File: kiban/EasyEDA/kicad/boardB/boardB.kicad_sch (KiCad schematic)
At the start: 0 parts

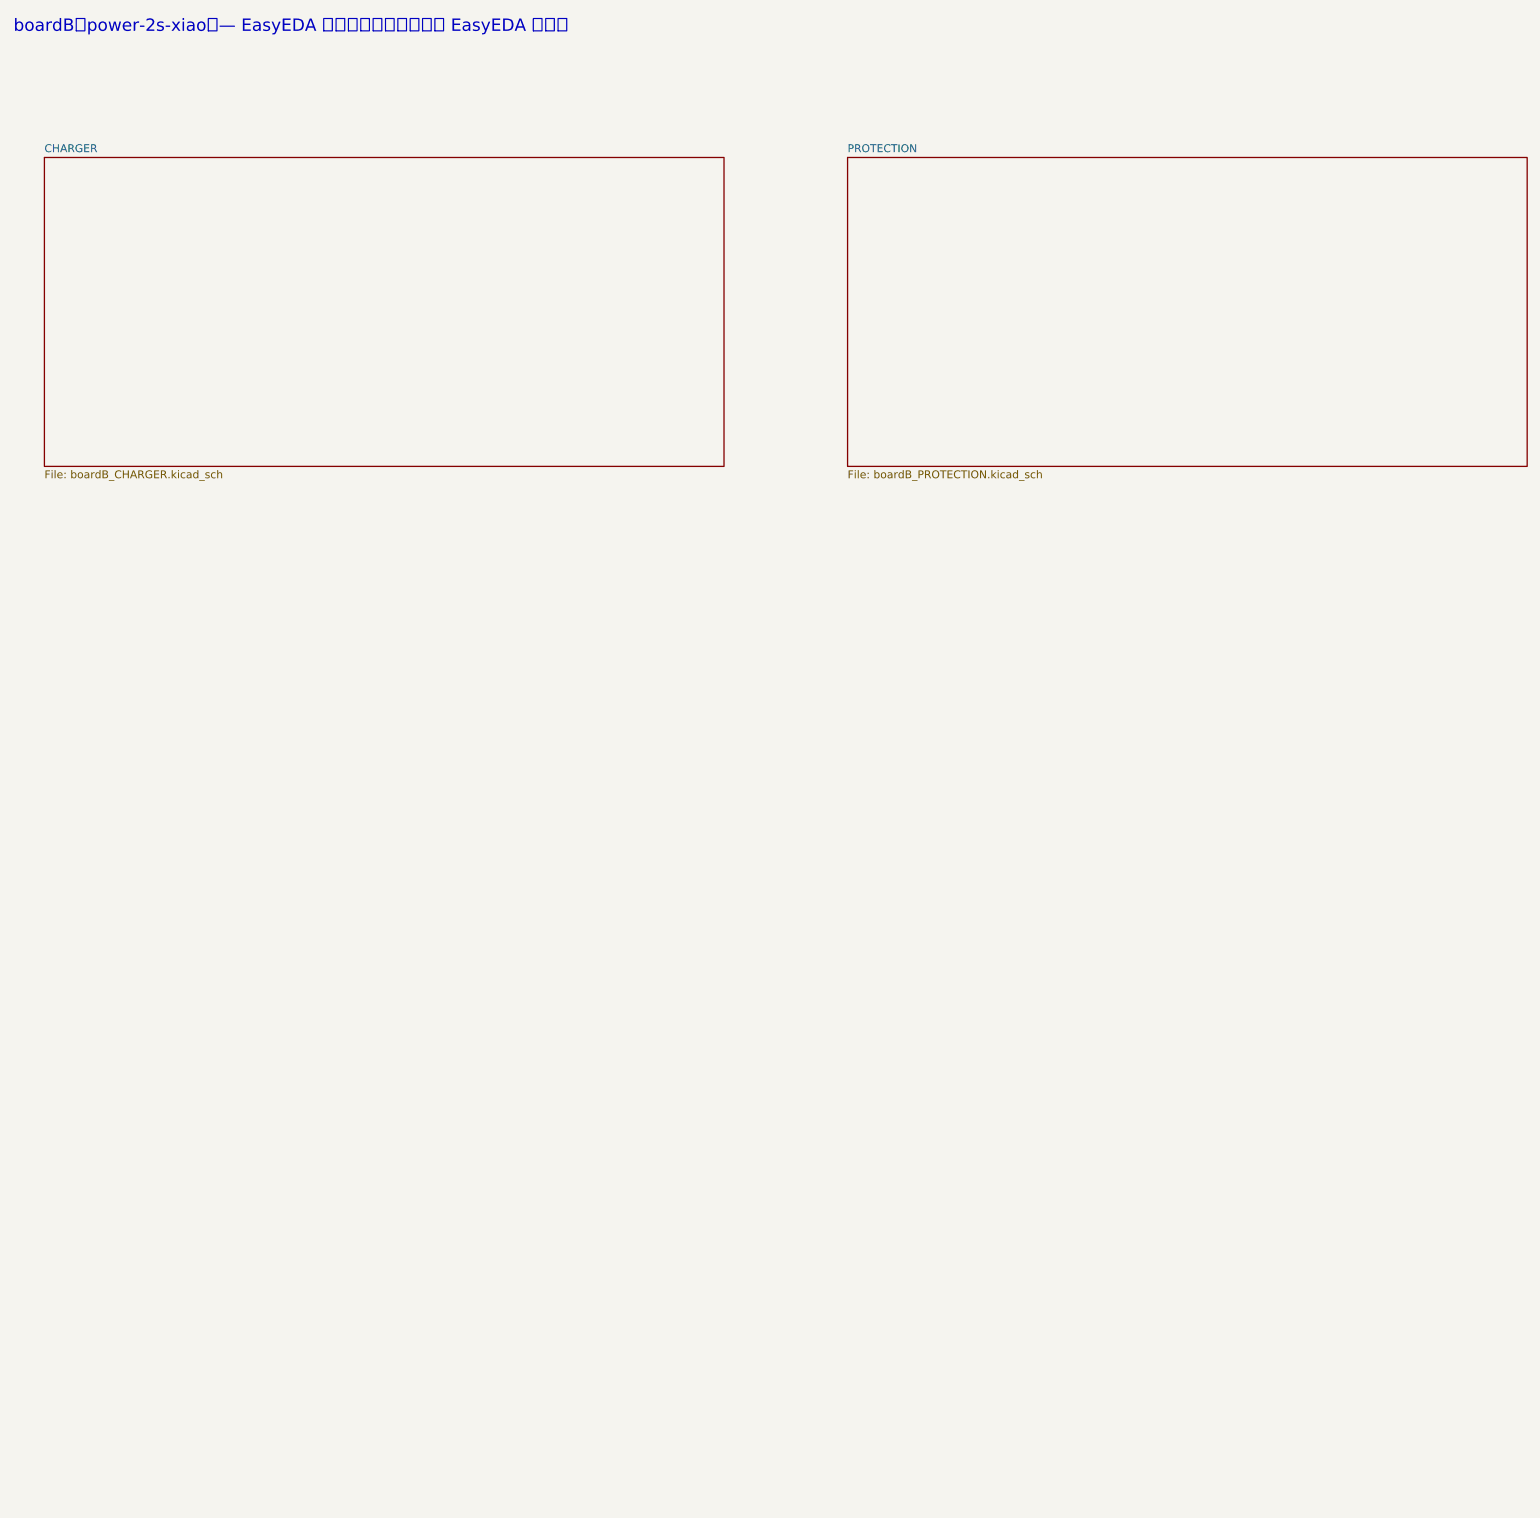
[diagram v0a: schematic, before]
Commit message: feat: 基板A / B の回路図を 1 枚に統合し、フットプリント・LCSC 品番・テストポイントを入れる
- 基板B: CHARGER と PROTECTION を手で 1 枚に統合 (KiCad が元データ)
- 基板A: kicad_flat.py で基板B と同じ書き方の 1 枚に作り直し、I2C プルアップ R9/R10 を削除、テストピン J5〜J10 を追加
- assign_footprints.py: LCSC 品番からフットプリントを割り当てる
- testpoints.py: テストパッドを回路図に追加する

Co-Authored-By: Claude Opus 5.5 <noreply@anthropic.com>
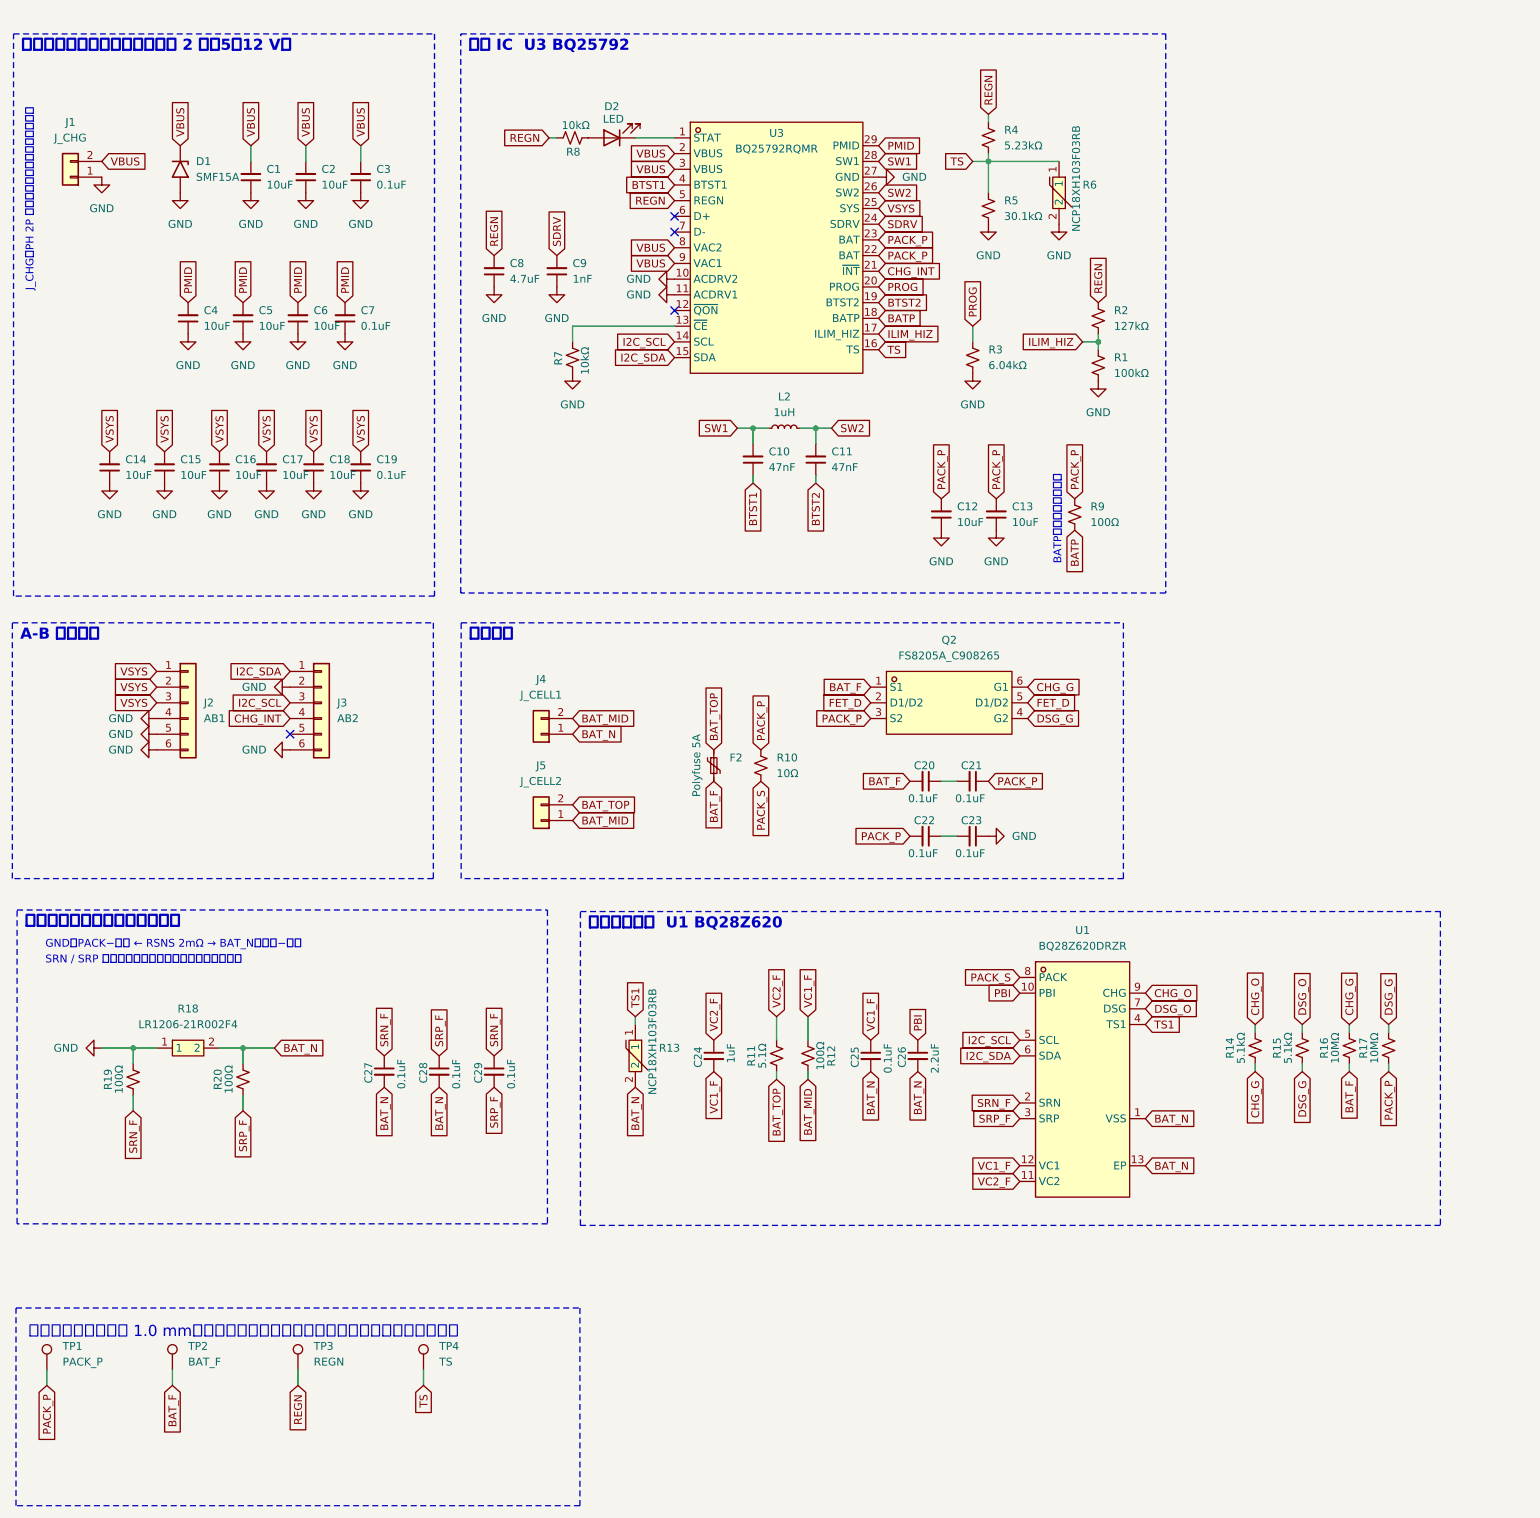
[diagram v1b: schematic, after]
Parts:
- added C1, C12, C13, C14, C15, C16, C17, C18, C2, C4, C5, C6: 10uF, lcsc:C0805, symbol Device:C_Small
- added C10, C11: 47nF, lcsc:C0603, symbol Device:C_Small
- added C19, C20, C21, C22, C23, C25, C27, C28, C29, C3, C7: 0.1uF, lcsc:C0603, symbol Device:C_Small
- added C24: 1uF, lcsc:C0603, symbol Device:C_Small
- added C26: 2.2uF, lcsc:C0603, symbol Device:C_Small
- added C8: 4.7uF, lcsc:C0603, symbol Device:C_Small
- added C9: 1nF, lcsc:C0603, symbol Device:C_Small
- added D1: SMF15A, lcsc:SOD-123FL_L2.8-W1.8-LS3.6-RD, symbol Diode:SMF15A
- added D2: LED, lcsc:LED-SMD_L1.6-W0.8-R-RD, symbol Device:LED
- added F2: Polyfuse 5A, lcsc:FUSE-SMD_L8.0-W5.4, symbol Device:Polyfuse_Small
- added J1: J_CHG, lcsc:HDR-TH_2P-P2.54-V-M, symbol Connector_Generic:Conn_01x02
- added J2: AB1, lcsc:HDR-TH_6P-P2.54-V-M, symbol Connector_Generic:Conn_01x06
- added J3: AB2, lcsc:HDR-TH_6P-P2.54-V-M, symbol Connector_Generic:Conn_01x06
- added J4: J_CELL1, lcsc:HDR-TH_2P-P2.54-V-M, symbol Connector_Generic:Conn_01x02
- added J5: J_CELL2, lcsc:HDR-TH_2P-P2.54-V-M, symbol Connector_Generic:Conn_01x02
- added L2: 1uH, lcsc:IND-SMD_L7.1-W6.5-P5.60, symbol Device:L_Small
- added Q2: FS8205A_C908265, lcsc:SOT-23-6_L2.9-W1.6-P0.95-LS2.8-BR, symbol lcsc:FS8205A_C908265
- added R1: 100kΩ, lcsc:R0603, symbol Device:R_Small_US
- added R10: 10Ω, lcsc:R0603, symbol Device:R_Small_US
- added R11: 5.1Ω, lcsc:R0603, symbol Device:R_Small_US
- added R12, R19, R20, R9: 100Ω, lcsc:R0603, symbol Device:R_Small_US
- added R13, R6: NCP18XH103F03RB, lcsc:R0603, symbol lcsc:NCP18XH103F03RB
- added R14, R15: 5.1kΩ, lcsc:R0603, symbol Device:R_Small_US
- added R16, R17: 10MΩ, lcsc:R0603, symbol Device:R_Small_US
- added R18: LR1206-21R002F4, lcsc:R1206, symbol lcsc:LR1206-21R002F4
- added R2: 127kΩ, lcsc:R0603, symbol Device:R_Small_US
- added R3: 6.04kΩ, lcsc:R0603, symbol Device:R_Small_US
- added R4: 5.23kΩ, lcsc:R0603, symbol Device:R_Small_US
- added R5: 30.1kΩ, lcsc:R0603, symbol Device:R_Small_US
- added R7, R8: 10kΩ, lcsc:R0603, symbol Device:R_Small_US
- added TP1: PACK_P, TestPoint:TestPoint_Pad_D1.0mm, symbol Connector:TestPoint
- added TP2: BAT_F, TestPoint:TestPoint_Pad_D1.0mm, symbol Connector:TestPoint
- added TP3: REGN, TestPoint:TestPoint_Pad_D1.0mm, symbol Connector:TestPoint
- added TP4: TS, TestPoint:TestPoint_Pad_D1.0mm, symbol Connector:TestPoint
- added U1: BQ28Z620DRZR, lcsc:SON-12_L4.0-W2.5-P0.40-TL-EP, symbol lcsc:BQ28Z620DRZR
- added U3: BQ25792RQMR, lcsc:QFN-29_L4.0-W4.0-P0.40-TL-BQ25792RQMR, symbol lcsc:BQ25792RQMR
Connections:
- new net: C20.1, C21.2
- new net: C22.1, C23.2
- new net: D2.1 (K), U3.1 (STAT)
- new net: D2.2 (A), R8.2
- new net: R7.1, U3.13 (~{CE})
- new net BATP: R9.2, U3.18 (BATP)
- new net BAT_F: C20.2, F2.2, Q2.1 (S1), R16.1, TP2.1
- new net BAT_MID: J4.2 (Pin_2), J5.1 (Pin_1), R12.2
- new net BAT_N: C25.2, C26.2, C27.2, C28.2, J4.1 (Pin_1), R13.2, R18.2, R20.2, U1.1 (VSS), U1.13 (EP)
- new net BAT_TOP: F2.1, J5.2 (Pin_2), R11.1
- new net BTST1: C10.1, U3.4 (BTST1)
- new net BTST2: C11.1, U3.19 (BTST2)
- new net CHG_G: Q2.6 (G1), R14.1, R16.2
- new net CHG_INT: J3.4 (Pin_4), U3.21 (~{INT})
- new net CHG_O: R14.2, U1.9 (CHG)
- new net DSG_G: Q2.4 (G2), R15.1, R17.2
- new net DSG_O: R15.2, U1.7 (DSG)
- new net FET_D: Q2.2 (D1/D2), Q2.5 (D1/D2)
- new net GND: C1.1, C12.1, C13.1, C14.1, C15.1, C16.1, C17.1, C18.1, C19.1, C2.1, C23.1, C3.1, C4.1, C5.1, C6.1, C7.1, C8.1, C9.1, D1.2 (A2), J1.1 (Pin_1), J2.4 (Pin_4), J2.5 (Pin_5), J2.6 (Pin_6), J3.2 (Pin_2), J3.6 (Pin_6), R1.2, R18.1, R19.2, R3.2, R5.2, R6.2, R7.2, U3.10 (ACDRV2), U3.11 (ACDRV1), U3.27 (GND)
- new net I2C_SCL: J3.3 (Pin_3), U1.5 (SCL), U3.14 (SCL)
- new net I2C_SDA: J3.1 (Pin_1), U1.6 (SDA), U3.15 (SDA)
- new net ILIM_HIZ: R1.1, R2.2, U3.17 (ILIM_HIZ)
- new net PACK_P: C12.2, C13.2, C21.1, C22.2, Q2.3 (S2), R10.1, R17.1, R9.1, TP1.1, U3.22 (BAT), U3.23 (BAT)
- new net PACK_S: R10.2, U1.8 (PACK)
- new net PBI: C26.1, U1.10 (PBI)
- new net PMID: C4.2, C5.2, C6.2, C7.2, U3.29 (PMID)
- new net PROG: R3.1, U3.20 (PROG)
- new net REGN: C8.2, R2.1, R4.1, R8.1, TP3.1, U3.5 (REGN)
- new net SDRV: C9.2, U3.24 (SDRV)
- new net SRN_F: C27.1, C29.1, R19.1, U1.2 (SRN)
- new net SRP_F: C28.1, C29.2, R20.1, U1.3 (SRP)
- new net SW1: C10.2, L2.1, U3.28 (SW1)
- new net SW2: C11.2, L2.2, U3.26 (SW2)
- new net TS: R4.2, R5.1, R6.1, TP4.1, U3.16 (TS)
- new net TS1: R13.1, U1.4 (TS1)
- new net VBUS: C1.2, C2.2, C3.2, D1.1 (A1), J1.2 (Pin_2), U3.2 (VBUS), U3.3 (VBUS), U3.8 (VAC2), U3.9 (VAC1)
- new net VC1_F: C24.2, C25.1, R12.1, U1.12 (VC1)
- new net VC2_F: C24.1, R11.2, U1.11 (VC2)
- new net VSYS: C14.2, C15.2, C16.2, C17.2, C18.2, C19.2, J2.1 (Pin_1), J2.2 (Pin_2), J2.3 (Pin_3), U3.25 (SYS)
- no-connect marks 0 -> 4
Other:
- removed sheet CHARGER
- removed sheet PROTECTION
- note added: "A-B コネクタ"
- note added: "BATP：電池の＋を検出"
- note added: "GND（PACK−）側 ← RSNS 2mΩ → BAT_N（セル−）側"
- note added: "J_CHG：PH 2P の線をはんだ付け（部品なし）"
- note added: "SRN / SRP はシャントの両端のパッドから直接取る"
- note added: "テストパッド（直径 1.0 mm、部品なし。コネクタのピンで測れないネットだけ）"
- note added: "主電流路"
- note added: "充電 IC U3 BQ25792"
- note added: "充電入力（線をはんだ付けする 2 穴、5〜12 V）"
- note added: "残量計・保護 U1 BQ28Z620"
- note added: "電流シャント（ケルビン接続）"
- note removed: "boardB（power-2s-xiao）— EasyEDA から自動生成。編集は EasyEDA で行う"

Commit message: feat: 基板B にテストピン (J10〜J14) を追加し、配線を修正。基板A の設定を更新
Co-Authored-By: Claude Opus 5.5 <noreply@anthropic.com>
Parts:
- removed TP1: PACK_P, TestPoint:TestPoint_Pad_D1.0mm, symbol Connector:TestPoint
- removed TP2: BAT_F, TestPoint:TestPoint_Pad_D1.0mm, symbol Connector:TestPoint
- removed TP3: REGN, TestPoint:TestPoint_Pad_D1.0mm, symbol Connector:TestPoint
- removed TP4: TS, TestPoint:TestPoint_Pad_D1.0mm, symbol Connector:TestPoint
- added J10: PACK_P, Connector_PinHeader_2.00mm:PinHeader_1x01_P2.00mm_Vertical, symbol Connector_Generic:Conn_01x01
- added J11: BAT_F, Connector_PinHeader_2.00mm:PinHeader_1x01_P2.00mm_Vertical, symbol Connector_Generic:Conn_01x01
- added J12: REGN, Connector_PinHeader_2.00mm:PinHeader_1x01_P2.00mm_Vertical, symbol Connector_Generic:Conn_01x01
- added J13: TS, Connector_PinHeader_2.00mm:PinHeader_1x01_P2.00mm_Vertical, symbol Connector_Generic:Conn_01x01
- added J14: VSYS, Connector_PinHeader_2.00mm:PinHeader_1x01_P2.00mm_Vertical, symbol Connector_Generic:Conn_01x01
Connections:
- net BAT_F: now also J11.1 (Pin_1)
- net PACK_P: now also J10.1 (Pin_1)
- net REGN: now also J12.1 (Pin_1)
- net TS: now also J13.1 (Pin_1)
- net VSYS: now also J14.1 (Pin_1)
